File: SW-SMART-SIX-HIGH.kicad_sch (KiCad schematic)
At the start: 90 parts, among them J1 SWLINK, J2 USART1, J3 POWER OUT, J4 POWER IN, J5 POWER OUT, SW0 BTS7002-1EPP, SW1 BTS7002-1EPP, SW2 BTS7002-1EPP, SW3 BTS7002-1EPP, SW4 BTS7002-1EPP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

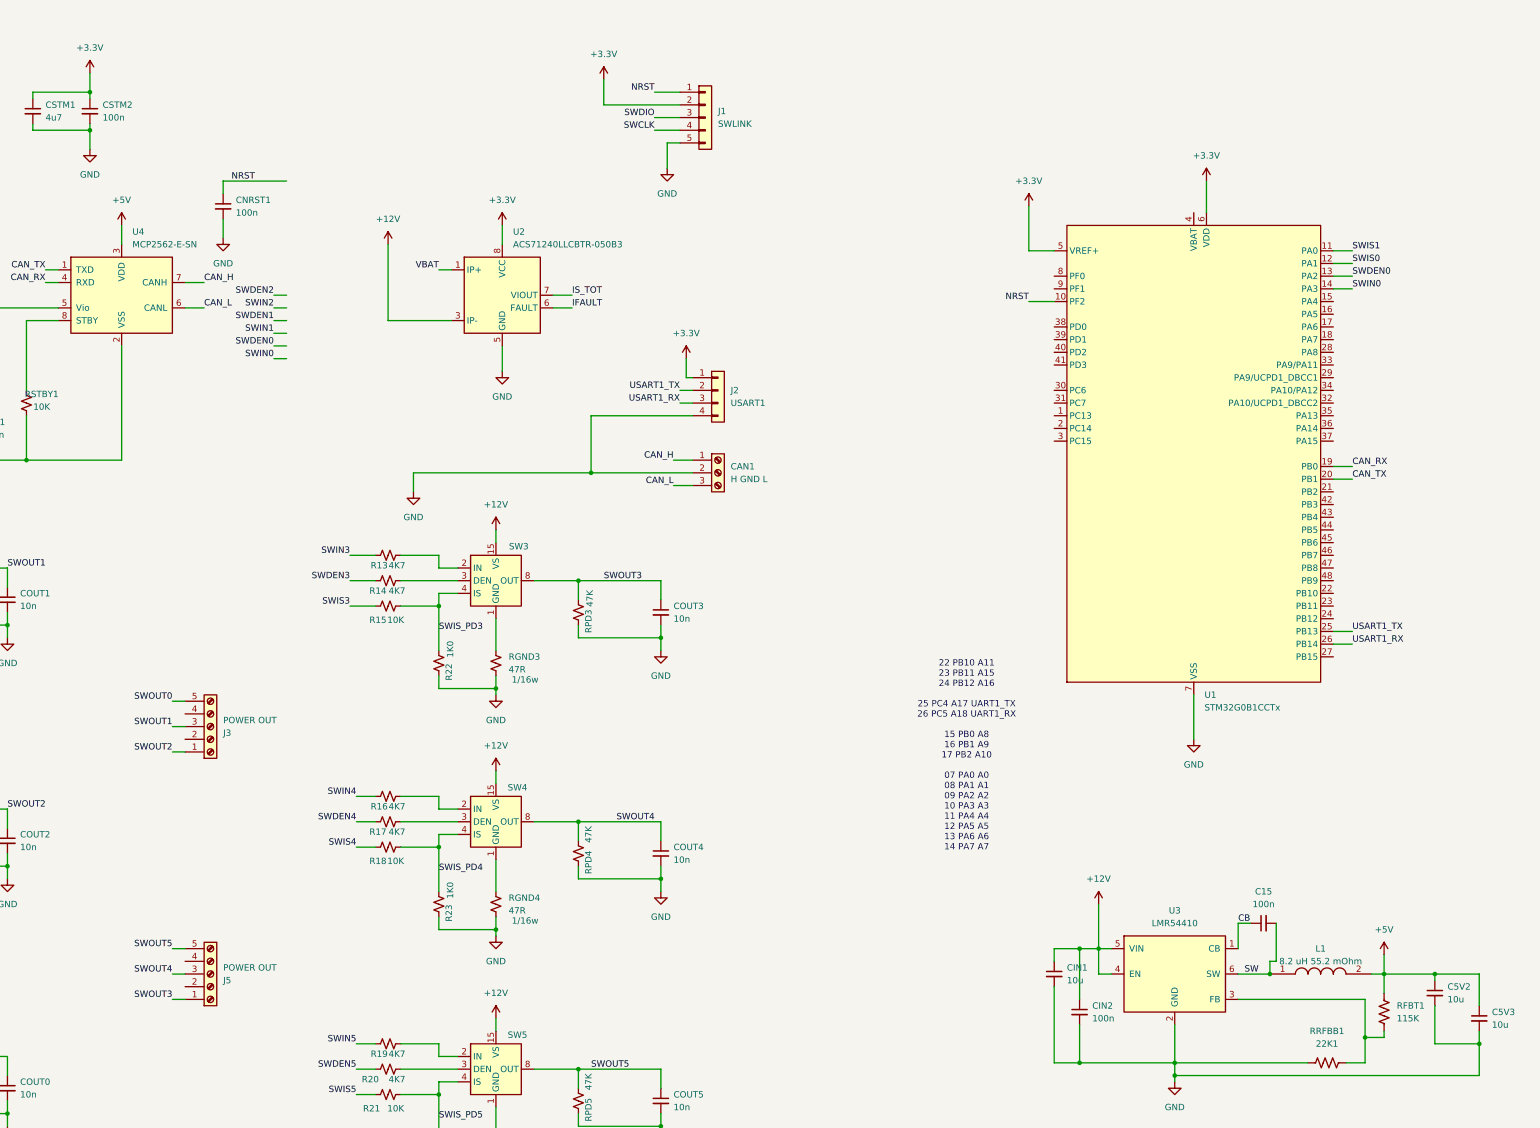
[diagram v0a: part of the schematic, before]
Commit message: update to the 64pin micro
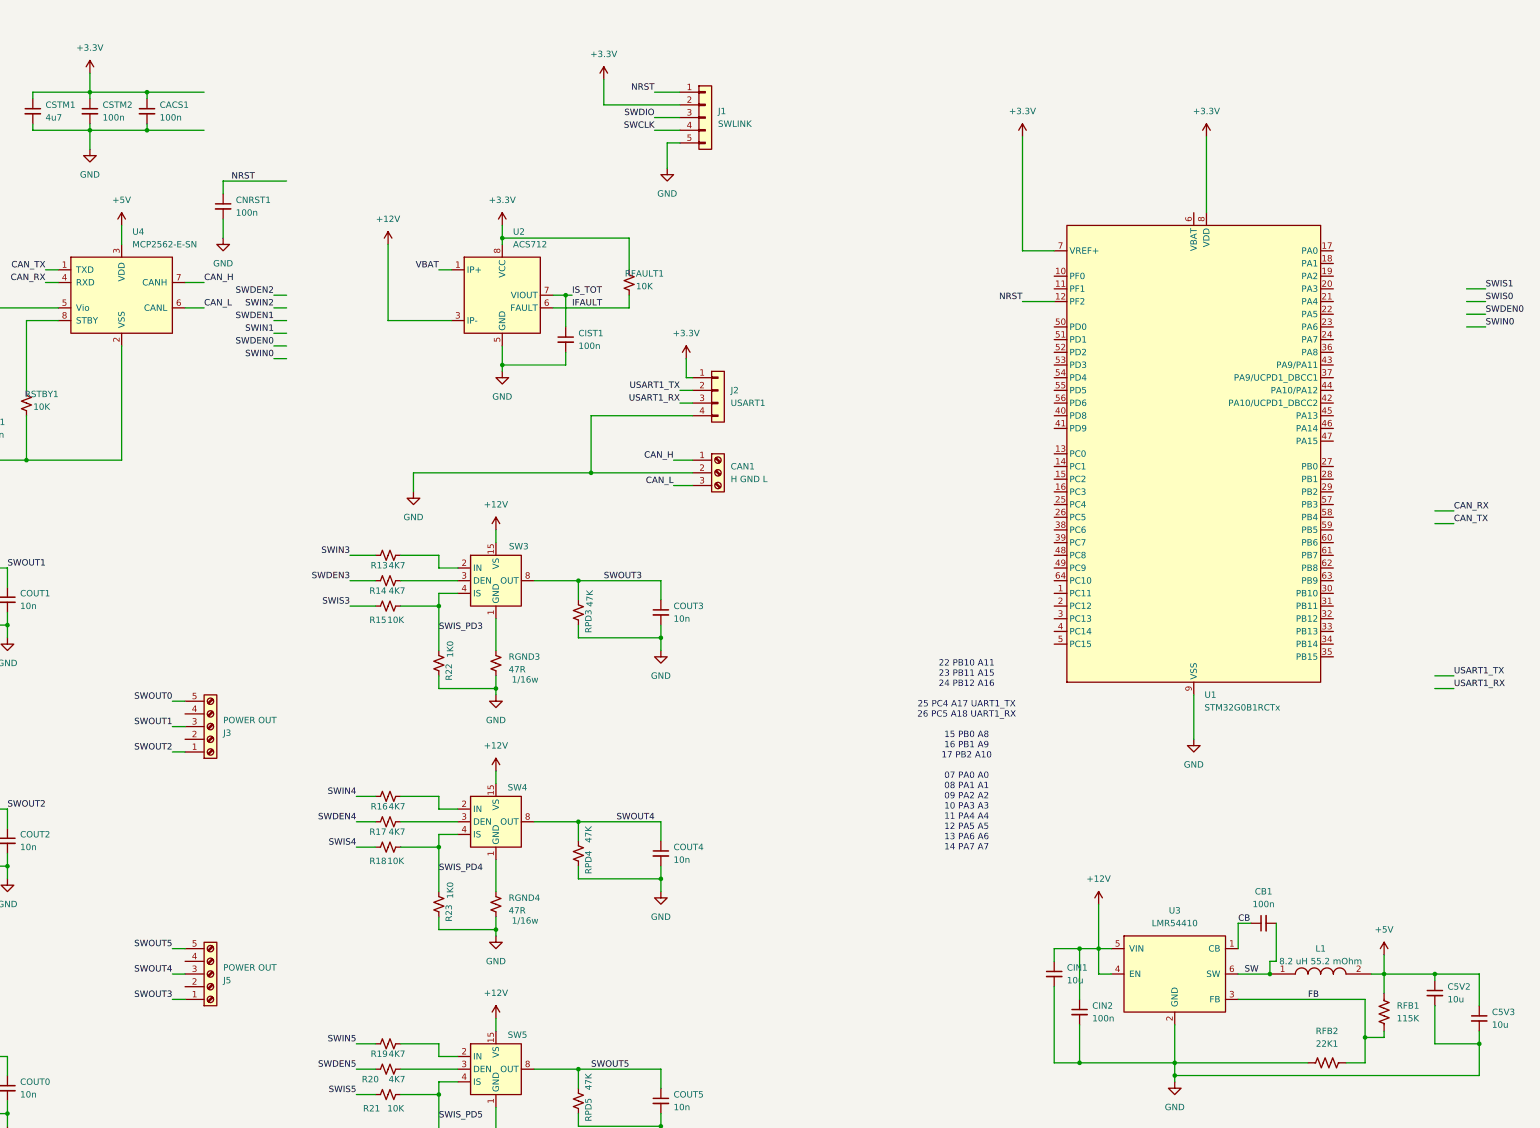
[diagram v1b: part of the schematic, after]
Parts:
- removed U1: STM32G0B1CCTx, Package_QFP:LQFP-48_7x7mm_P0.5mm, symbol MCU_ST_STM32G0:STM32G0B1CCTx
- added CACS1, CIST1: 100n, Capacitor_SMD:C_0603_1608Metric_Pad1.08x0.95mm_HandSolder, symbol Device:C_Small
- added RFAULT1: 10K, Resistor_SMD:R_0603_1608Metric_Pad0.98x0.95mm_HandSolder, symbol Device:R_Small_US
- added U1: STM32G0B1RCTx, Package_QFP:LQFP-64_10x10mm_P0.5mm, symbol MCU_ST_STM32G0:STM32G0B1RCTx
- U2: value ACS71240LLCBTR-050B3 -> ACS712; Part Number (none) -> ACS71240LLCBTR-050B3
- renumbered C15 to CB1, RFBT1 to RFB1, RRFBB1 to RFB2
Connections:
- net +3.3V: now also CACS1.1, RFAULT1.2, U1.7 (VREF+), U1.8 (VDD)
- net GND: now also CACS1.2, CIST1.2, U1.9 (VSS)
- net IFAULT: now also RFAULT1.1
- net IS_TOT: now also CIST1.1
- net NRST: now also U1.12 (PF2)
- net FB: now reaches RFB1.2, RFB2.2, U3.3 (FB)

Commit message: great progress with routing so far
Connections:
- net SWDEN0: now also U1.27 (PB0)
- net SWDEN1: now also U1.21 (PA4)
- net SWDEN2: now also U1.18 (PA1)
- net SWIN0: now also U1.28 (PB1)
- net SWIN1: now also U1.22 (PA5)
- net SWIN2: now also U1.19 (PA2)
- net SWIS0: now also U1.26 (PC5)
- net SWIS1: now also U1.20 (PA3)
- net SWIS2: now also U1.17 (PA0)
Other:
- note removed: "22 PB10 A11 23 PB11 A15 24 PB12 A16 25 PC4 A17 UART1_TX 26 PC5 A18 UART1_RX 15 PB0 A8 16 PB1 A9 17 PB2 A10 07 PA0 A0 08 PA1 A1 09 PA2 A2 10 PA3 A3 11 PA4 A4 12 PA5 A5 13 PA6 A6 14 PA7 A7"

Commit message: signals routed, next is power
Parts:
- J2: value USART1 -> USART2
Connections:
- net USART1_RX is gone; now on net USART2_RX: J2.3 (Pin_3)
- net USART1_TX is gone; now on net USART2_TX: J2.2 (Pin_2)
- net CAN_RX: now also U1.50 (PD0)
- net CAN_TX: now also U1.51 (PD1)
- net IS_TOT: now also U1.27 (PB0)
- net SWCLK: now also U1.46 (PA14)
- net SWDEN0: now also U1.24 (PA7); no longer U1.27 (PB0)
- net SWDEN3: now also U1.33 (PB13)
- net SWDEN4: now also U1.35 (PB15)
- net SWDEN5: now also U1.38 (PC6)
- net SWDIO: now also U1.45 (PA13)
- net SWIN0: now also U1.25 (PC4); no longer U1.28 (PB1)
- net SWIN3: now also U1.34 (PB14)
- net SWIN4: now also U1.36 (PA8)
- net SWIN5: now also U1.39 (PC7)
- net SWIS0: now also U1.23 (PA6); no longer U1.26 (PC5)
- net SWIS3: now also U1.28 (PB1)
- net SWIS4: now also U1.29 (PB2)
- net SWIS5: now also U1.30 (PB10)
- net VS: now also U1.26 (PC5)
- net USART2_TX: now reaches U1.55 (PD5)
- net USART2_RX: now reaches U1.56 (PD6)
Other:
- moved on the sheet: J1

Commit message: Schematic cleanup and documentation
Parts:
- added D2: STAT1, LED_SMD:LED_0805_2012Metric_Pad1.15x1.40mm_HandSolder, symbol Device:LED
- added D3: STAT2, LED_SMD:LED_0805_2012Metric_Pad1.15x1.40mm_HandSolder, symbol Device:LED
- added R25, R26: 1K0, Resistor_SMD:R_0603_1608Metric_Pad0.98x0.95mm_HandSolder, symbol Device:R_Small_US
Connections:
- net +3.3V: no longer C3V1.1, U4.5 (Vio)
- net GND: now also R25.1, R26.1
- net STAT1: now reaches U1.40 (PD8)
- net STAT1: now also D2.2 (A)
- net STAT2: now reaches U1.41 (PD9)
- new net: D3.1 (K), R26.2
- new net: D2.1 (K), R25.2
- new net: C3V1.1, U4.5 (Vio)
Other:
- note added: "5v switch mode power supply section"
- note added: "Infineon PROFet Automotive High-side Switches"
- note added: "Isolated CAN bus transceiver"
- note added: "STM32 Microcontroller and external interface connectors"
- note added: "Total board current monitor"
- moved on the sheet: C3V1, CAN1, CIST1, CNRST1, J1, J2, RFAULT1, RSTBY1, U1, U2, U4

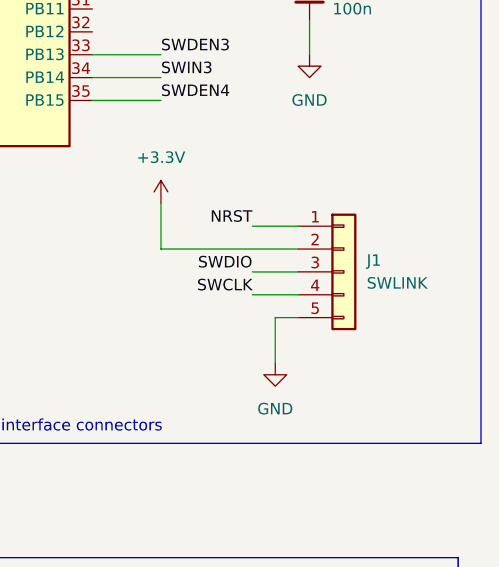
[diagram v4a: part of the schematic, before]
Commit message: rename swlink to swd
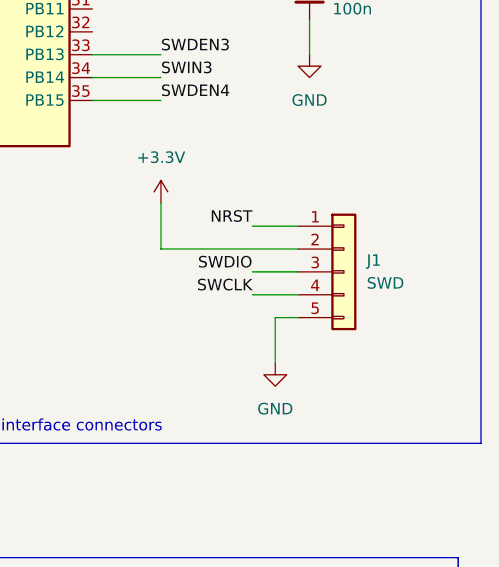
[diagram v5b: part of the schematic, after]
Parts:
- J1: value SWLINK -> SWD
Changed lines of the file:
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@@
 			)
 		)
-		(property "Value" "SWLINK"
+		(property "Value" "SWD"
 			(at 402.59 147.3199 0)
 			(effects

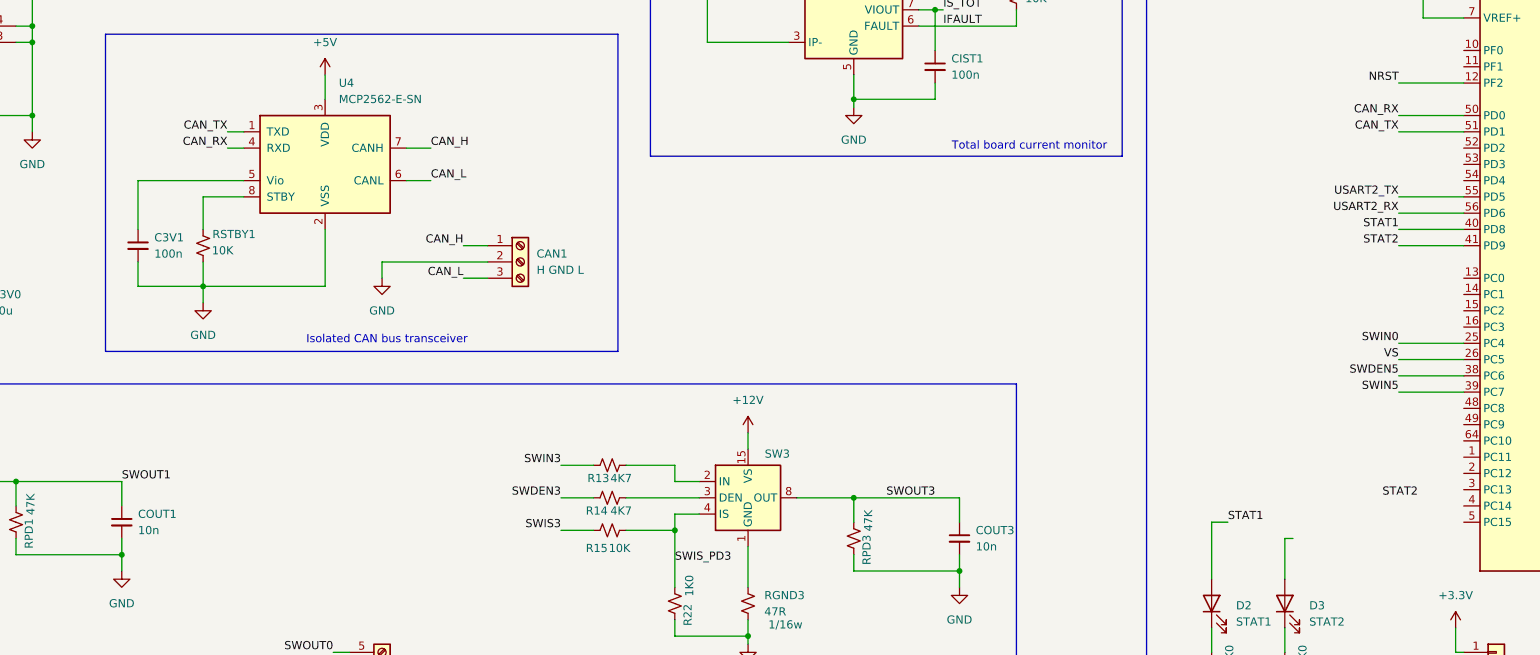
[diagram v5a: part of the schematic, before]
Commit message: fix a few issues that cropped up
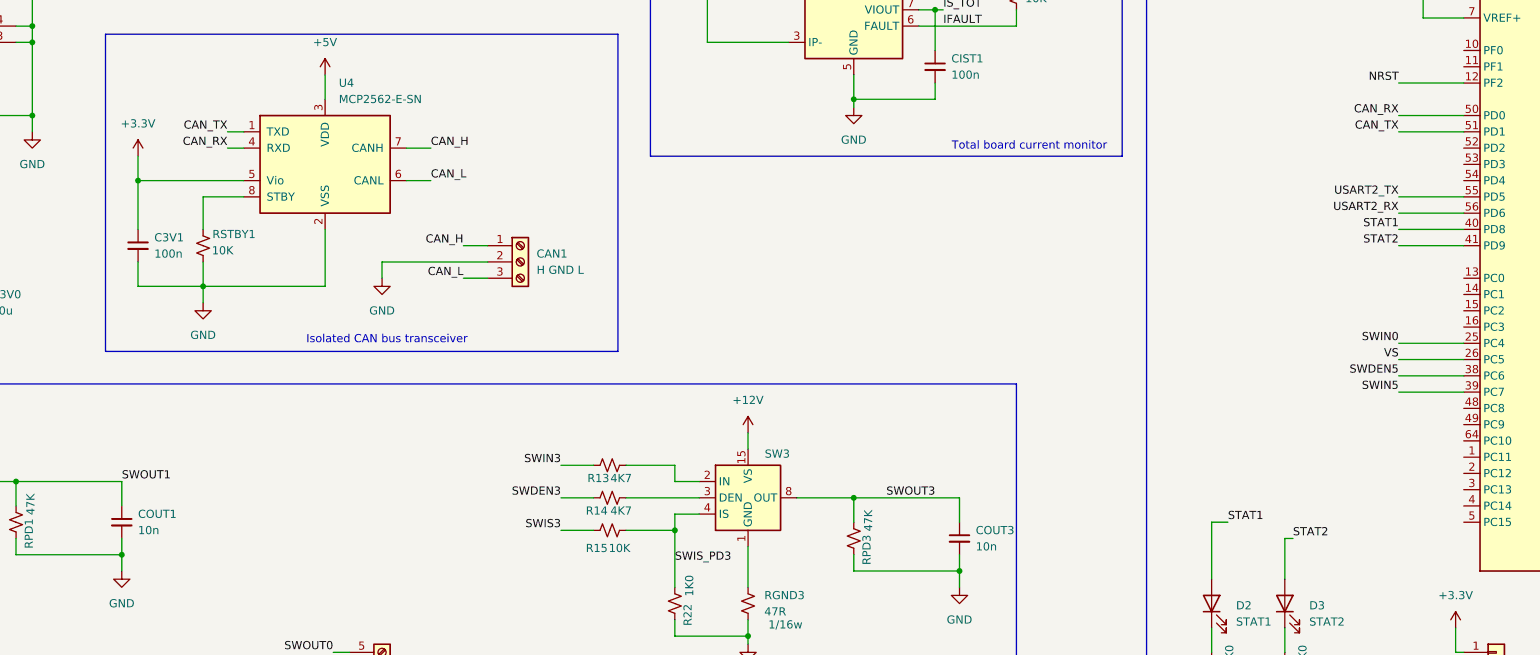
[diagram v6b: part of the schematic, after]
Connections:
- net +3.3V: now also C3V1.1, U4.5 (Vio)
- net STAT2: now also D3.2 (A)
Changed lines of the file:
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@@
 	)
 	(junction
+		(at 109.22 71.12)
+		(diameter 0)
+		(color 0 0 0 0)
+	)
+	(junction
 		(at 220.98 168.91)
 		(diameter 0)
@@
 	(wire
 		(pts
+			(xy 109.22 67.31) (xy 109.22 71.12)
+		)
+		(stroke
+			(width 0)
+			(type default)
+		)
+	)
+	(wire
+		(pts
 			(xy 193.04 125.73) (xy 193.04 134.62)
 		)
@@
 	)
 	(label "STAT2"
-		(at 303.53 120.65 0)
+		(at 289.56 127 0)
 		(effects
 			(font
@@
 					(unit 1)
 				)
+			)
+		)
+	)
+	(symbol
+		(lib_id "power:+3.3V")
+		(at 109.22 67.31 0)
+		(unit 1)
+		(exclude_from_sim no)
+		(in_bom yes)
+		(on_board yes)
+		(dnp no)
+		(property "Reference" "#PWR044"
+			(at 109.22 71.12 0)
+			(effects
+				(font
+					(size 1.27 1.27)
+				)
+				(hide yes)
+			)
+		)
+		(property "Value" "+3.3V"
+			(at 109.22 62.23 0)
+			(effects
+				(font
+					(size 1.27 1.27)
+				)
+			)
+		)
+		(property "Footprint" ""
+			(at 109.22 67.31 0)
+			(effects
+				(font
+					(size 1.27 1.27)
+				)
+				(hide yes)
+			)
+		)
+		(property "Datasheet" ""
+			(at 109.22 67.31 0)
+			(effects
+				(font
+					(size 1.27 1.27)
+				)
+				(hide yes)
+			)
+		)
+		(property "Description" "Power symbol creates a global label with name \"+3.3V\""
+			(at 109.22 67.31 0)
+			(effects
+				(font
+					(size 1.27 1.27)
+				)
+				(hide yes)
+			)
+		)
+		(pin "1"
+		)
+		(instances
+			(project "SW-SMART-SIX-HIGH"
+				(path "/08d9f551-d314-4c5c-859f-da02a807087d"
+					(reference "#PWR044")
+					(unit 1)
+				)

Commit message: added dedicated board temperature sensor
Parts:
- added U5: MCP9700Ax-ETT, Package_TO_SOT_SMD:SOT-23, symbol Sensor_Temperature:MCP9700Ax-ETT
- L1: footprint SRP5030HMT2R2M -> SRP5030HMT-8R2M
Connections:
- net GND: now also U5.3 (GND)
- net BRDTMP: now reaches U1.32 (PB12)
- net BRDTMP: now also U5.2 (V_{OUT})
- net TMP_PWR: now reaches U1.37 (PA9/UCPD1_DBCC1)
- net TMP_PWR: now also U5.1 (V_{DD})
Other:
- note added: "5v switch mode power supply"
- note added: "Board temperature sensor"
- note added: "Decoupling and bulk caps"
- note added: "Linear 3.3v supply"
- note added: "Main power input and various passive components"
- note removed: "5v switch mode power supply section"
- moved on the sheet: C3V0, C5V0, C5V1, CACS1, COUT0, COUT1, COUT2, COUT3, COUT4, COUT5, CSTM1, CSTM2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
